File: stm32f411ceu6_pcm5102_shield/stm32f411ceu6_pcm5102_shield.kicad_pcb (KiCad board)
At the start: 2 copper layers, 78 parts, among them J100 Conn_01x04_Pin, J101 Conn_01x04_Pin, J200 AudioJack3_Ground_SwitchTR, J300 AudioJack3_Ground_SwitchTR, Q300 BC337, Q301 BC337, SW100 RotaryEncoder_Switch_MP, SW200 SW_DPDT_XLX, SW201 SW_DPDT_XLX, SW202 SW_DPDT_XLX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

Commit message: Put all items on a board
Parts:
- removed R203: 100kR, Resistor_SMD:R_0805_2012Metric
- removed R204: 10R, Resistor_SMD:R_0805_2012Metric
- J200, J300: footprint Connector_Audio:Jack_3.5mm_PJ311_Horizontal -> stm32f401_pcm5102_shiled_lib:AudioJack_3.5mm_PJ311
- SW101, SW102, SW103, SW104: footprint Button_Switch_THT:SW_PUSH_6mm -> stm32f401_pcm5102_shiled_lib:SW_PUSH_6mm_H5mm
- moved J200 59.2 mm to (193.5, 111.9)
- moved J300 44.1 mm to (192.8, 91.4)
- moved U200 39.3 mm to (144.1, 94.4)
- moved R304 35.6 mm to (168.9, 82.9)
- moved R309 32.7 mm to (173.3, 85.8)
- moved R308 32.7 mm to (173.3, 82.9)
- moved L200 31.1 mm to (146.9, 99.4)
- moved C205 30.3 mm to (136.5, 92.0)
- moved C207 30.3 mm to (136.5, 95.1)
- moved C209 30.3 mm to (136.5, 98.3)
- moved C211 30.3 mm to (136.5, 101.4)
- moved C213 28.8 mm to (131.4, 91.9)
- moved C214 28.8 mm to (131.4, 94.9)
- moved C215 28.8 mm to (131.4, 97.9)
- moved C216 28.8 mm to (131.4, 100.9)
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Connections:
- SW101 pad 1: USR_MIC_MUTE_BTN -> +3.3V
- SW101 pad 2: +3.3V -> USR_MIC_MUTE_BTN
- SW102 pad 1: USR_SCAN_NEXT_BTN -> +3.3V
- SW102 pad 2: +3.3V -> USR_SCAN_NEXT_BTN
- SW103 pad 1: USR_SCAN_PREV_BTN -> +3.3V
- SW103 pad 2: +3.3V -> USR_SCAN_PREV_BTN
- SW104 pad 1: USR_PLAY_PAUSE_BTN -> +3.3V
- SW104 pad 2: +3.3V -> USR_PLAY_PAUSE_BTN

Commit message: PCB rules setup
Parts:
- added J201: Conn_01x03_Pin, Connector_PinHeader_2.54mm:PinHeader_1x03_P2.54mm_Vertical, F.Cu at (129.4, 120.5)
- added J301: Conn_01x03_Pin, Connector_PinHeader_2.54mm:PinHeader_1x03_P2.54mm_Vertical, F.Cu at (141.3, 127.8)
- C100, C101, C102, C204, C206, C208, C210: footprint Capacitor_SMD:C_0805_2012Metric -> Capacitor_SMD:C_0402_1005Metric
- moved J200 91.7 mm to (102.5, 123.0)
- moved D1 59.1 mm to (113.1, 102.5)
- moved J300 53.4 mm to (144.5, 114.0)
- moved L200 53.3 mm to (109.5, 137.3)
- moved U201 44.6 mm to (111.4, 133.3)
- moved C100 43.6 mm to (147.8, 93.0)
- moved C101 42.5 mm to (147.8, 95.0)
- moved C102 41.5 mm to (147.8, 97.0)
- moved U200 39.4 mm to (131.8, 131.8)
- moved C302 30.3 mm to (152.9, 128.8)
- moved R202 30.3 mm to (94.8, 137.3)
- moved SW100 30.3 mm to (124.0, 81.7)
- moved C201 30.3 mm to (110.2, 122.6)
- moved C202 30.3 mm to (110.2, 125.7)
- moved C205 30.3 mm to (124.2, 119.7)
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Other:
- copper layers 2 -> 4
- rule pad_to_mask_clearance: 0 -> 0.038

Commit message: Initial layout
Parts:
- removed C204, C206, C208: 100nF, Capacitor_SMD:C_0402_1005Metric
- removed C205, C207, C209: 10uF, Capacitor_Tantalum_SMD:CP_EIA-3216-18_Kemet-A
- added C1: 100nF, Capacitor_SMD:C_0402_1005Metric, F.Cu at (104.0, 103.5)
- added C2: 100nF, Capacitor_SMD:C_0402_1005Metric, F.Cu at (114.2, 103.8)
- added C3: 100nF, Capacitor_SMD:C_0402_1005Metric, F.Cu at (104.0, 110.1)
- added C4: 10uF, Capacitor_Tantalum_SMD:CP_EIA-3216-18_Kemet-A, F.Cu at (100.8, 103.5)
- added C5: 10uF, Capacitor_Tantalum_SMD:CP_EIA-3216-18_Kemet-A, F.Cu at (117.5, 103.8)
- added C6: 10uF, Capacitor_Tantalum_SMD:CP_EIA-3216-18_Kemet-A, F.Cu at (100.8, 110.1)
- moved R311 68.8 mm to (94.3, 102.6), turned to -90 degrees
- moved R308 67.6 mm to (94.5, 122.3)
- moved R310 67.1 mm to (94.1, 110.9), turned to 90 degrees
- moved R309 67.0 mm to (94.3, 119.8)
- moved J300 63.5 mm to (81.3, 120.9), turned to 90 degrees
- moved C101 58.9 mm to (109.9, 49.9)
- moved R306 58.6 mm to (98.1, 120.7), turned to 90 degrees
- moved C303 58.1 mm to (96.7, 116.9)
- moved Q301 56.3 mm to (102.4, 119.4), turned to 90 degrees
- moved C301 55.9 mm to (97.0, 125.0), turned to 180 degrees
- moved Q300 55.5 mm to (102.3, 127.7), turned to 90 degrees
- moved R302 55.3 mm to (98.2, 128.2), turned to 90 degrees
- moved C102 54.8 mm to (120.4, 49.5)
- moved R307 54.1 mm to (102.7, 114.1)
- moved J301 54.1 mm to (87.2, 128.3), turned to -90 degrees
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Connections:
- SW101 pad 1: +3.3V -> USR_MIC_MUTE_BTN
- SW101 pad 2: USR_MIC_MUTE_BTN -> +3.3V
- SW102 pad 1: +3.3V -> USR_SCAN_NEXT_BTN
- SW102 pad 2: USR_SCAN_NEXT_BTN -> +3.3V
- SW103 pad 1: +3.3V -> USR_SCAN_PREV_BTN
- SW103 pad 2: USR_SCAN_PREV_BTN -> +3.3V
- SW104 pad 1: +3.3V -> USR_PLAY_PAUSE_BTN
- SW104 pad 2: USR_PLAY_PAUSE_BTN -> +3.3V
- U101 pad 1: +3.3V -> +3.3VA
- U200 pad 20: +3.3V -> +3.3VA
- U200 pad 8: +3.3VA -> +3.3V

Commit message: Initial layout
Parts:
- removed Brd100: SSD1306, stm32f401_pcm5102_shiled_lib:128x64OLED
- removed SW201, SW202, SW203, SW204: SW_DPDT_XLX, stm32f401_pcm5102_shiled_lib:SW_DPDT_XLX
- added J102: Conn_01x04_Pin, Connector_PinHeader_2.54mm:PinHeader_1x04_P2.54mm_Vertical, F.Cu at (104.9, 98.8)
- moved D1 86.2 mm to (82.2, 58.0)
- moved R110 80.4 mm to (85.7, 58.0), turned to 0 degrees
- moved U101 66.7 mm to (83.0, 68.1), turned to 180 degrees
- moved J101 44.7 mm to (87.1, 98.8), turned to 90 degrees
- moved C203 39.1 mm to (125.5, 126.5), turned to -90 degrees
- moved C202 29.8 mm to (122.5, 125.7), turned to 180 degrees
- moved U201 23.9 mm to (123.2, 121.5), turned to 90 degrees
- moved R105 20.0 mm to (92.5, 53.2)
- moved R107 19.6 mm to (117.7, 75.8), turned to 0 degrees
- moved R108 19.6 mm to (117.9, 52.5), turned to 0 degrees
- moved R200 19.1 mm to (122.5, 118.0), turned to 180 degrees
- moved R109 18.9 mm to (109.9, 75.8), turned to 0 degrees
- moved R106 18.7 mm to (110.7, 52.5), turned to 0 degrees
- moved SW103 18.6 mm to (116.7, 62.2)
- moved SW102 18.5 mm to (116.7, 72.2)
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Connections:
- U100 pad 26: I2C1_SDA -> /MCU/I2C1_SDA
- U100 pad 27: I2C1_SCL -> /MCU/I2C1_SCL
- U200 pad 10: /PCM5102/DEMP_CFG -> GND
- U200 pad 11: /PCM5102/FLT_CFG -> GND
- U200 pad 16: /PCM5102/FMT_CFG -> GND
- U200 pad 17: /PCM5102/XSMT_CFG -> +3.3V

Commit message: Board outline
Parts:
- added H1: MountingHole, MountingHole:MountingHole_3.2mm_M3, F.Cu at (80.2, 55.0)
- added H2: MountingHole, MountingHole:MountingHole_3.2mm_M3, F.Cu at (130.2, 55.0)
- added H3: MountingHole, MountingHole:MountingHole_3.2mm_M3, F.Cu at (130.2, 132.5)
- added H4: MountingHole, MountingHole:MountingHole_3.2mm_M3, F.Cu at (80.2, 132.5)
- moved R110 5.41 mm to (86.8, 52.7), turned to 90 degrees
- moved D1 4.86 mm to (86.8, 56.2), turned to -90 degrees
- moved SW200 1.58 mm to (127.5, 108.2)
- moved J301 1.00 mm to (82.5, 115.2)
- moved C200 0.99 mm to (121.0, 97.7)
- moved C201 0.99 mm to (121.0, 99.9)
- moved L200 0.99 mm to (118.5, 98.7)
- moved J300 0.96 mm to (79.8, 123.0)
- moved J200 0.77 mm to (79.8, 107.9)
- moved C100 0.77 mm to (98.2, 75.4)
- moved C202 0.77 mm to (122.0, 125.1)
- moved C203 0.77 mm to (125.0, 125.9)
- moved J101 0.77 mm to (86.6, 98.2)
- moved J102 0.77 mm to (104.4, 98.2)
- moved R100 0.77 mm to (95.9, 74.4)
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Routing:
- net Net-(J100-Pin_4): track 0.00 -> 7.95 mm
- net Net-(J100-Pin_3): track 0.00 -> 7.95 mm
- net Net-(J100-Pin_2): track 0.00 -> 7.95 mm
- net Net-(J100-Pin_1): track 0.00 -> 7.95 mm
- net +5V: track 0.00 -> 5.59 mm
- net /MCU/I2C1_SCL: track 0.00 -> 4.25 mm
- net /MCU/I2C1_SDA: track 0.00 -> 4.25 mm
- net /MCU/USART1_RX: track 0.00 -> 4.24 mm
- net /MCU/USART1_TX: track 0.00 -> 4.24 mm
- net GND: track 0.00 -> 3.70 mm
- net +5VA: track 0.00 -> 2.02 mm
- added copper zone on In1.Cu, net GND
- added copper zone on In2.Cu, net GND
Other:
- board outline added: 60 x 87.5 mm

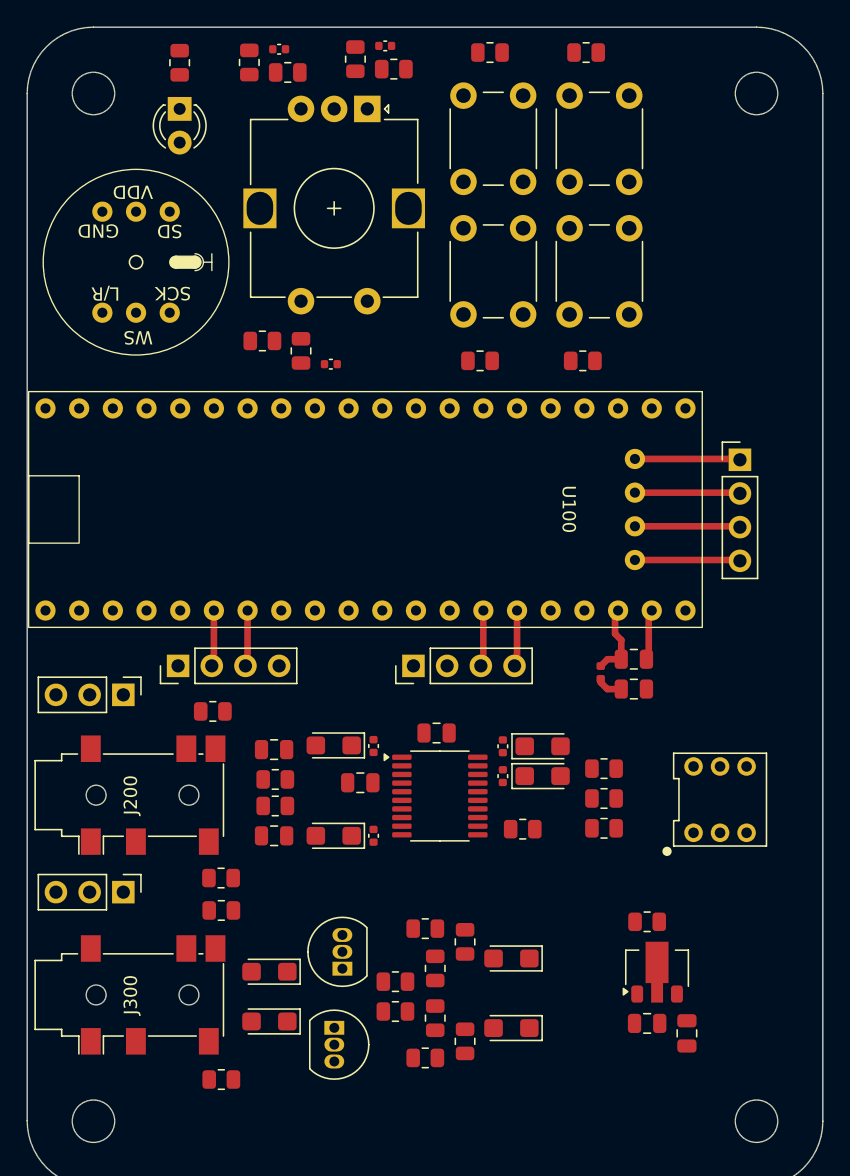
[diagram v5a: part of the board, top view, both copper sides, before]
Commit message: First PCB routing
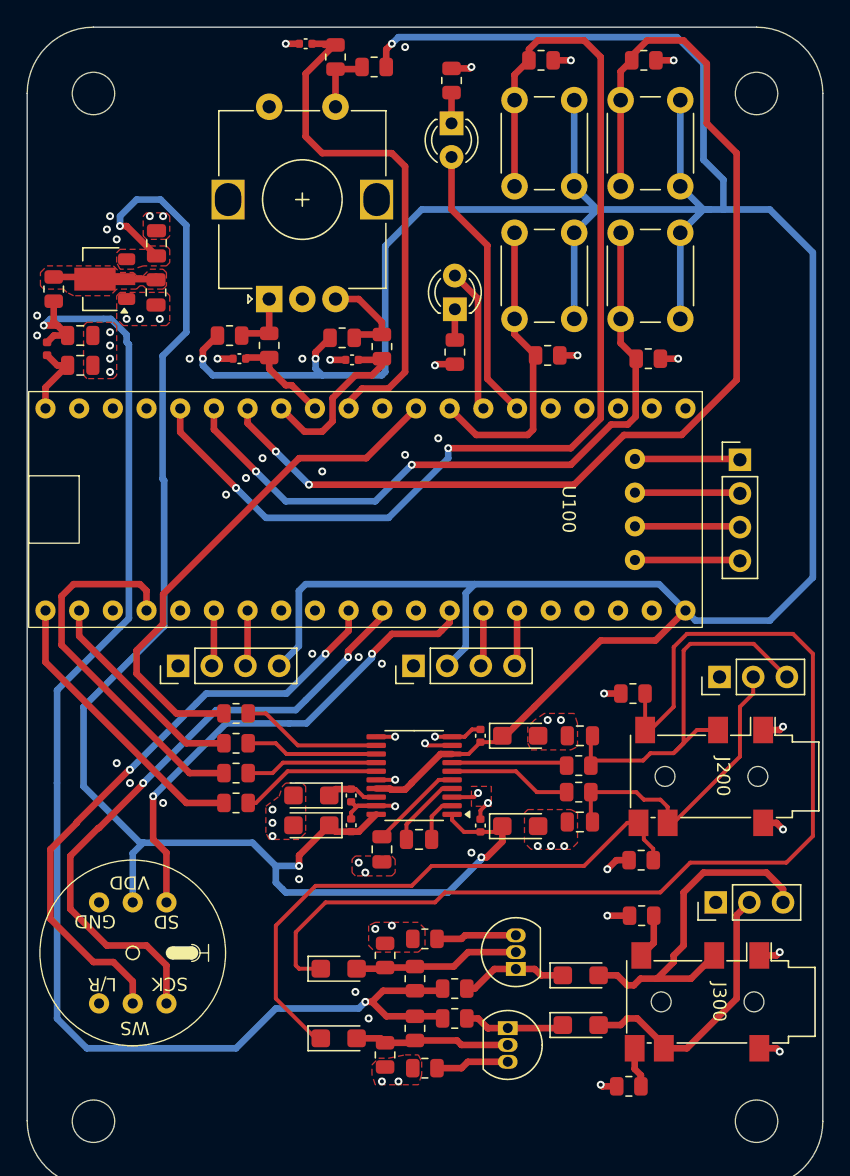
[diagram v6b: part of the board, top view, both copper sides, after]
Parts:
- removed SW200: SW_DPDT_XLX, stm32f401_pcm5102_shiled_lib:SW_DPDT_XLX
- added D101: LED, LED_THT:LED_D3.0mm, F.Cu at (107.2, 57.2)
- added R111: 1kR, Resistor_SMD:R_0805_2012Metric, F.Cu at (107.2, 54.0)
- moved C203 71.8 mm to (85.0, 66.3), turned to 90 degrees
- moved U201 66.8 mm to (80.8, 69.0), turned to 180 degrees
- moved C202 66.4 mm to (85.0, 70.0), turned to -90 degrees
- moved R200 65.4 mm to (77.2, 69.8), turned to -90 degrees
- moved U101 52.1 mm to (83.2, 119.8)
- moved J200 51.3 mm to (131.0, 106.5), turned to -90 degrees
- moved J300 51.0 mm to (130.8, 123.5), turned to -90 degrees
- moved C201 49.5 mm to (79.2, 73.2)
- moved L200 48.4 mm to (76.8, 74.2), turned to 90 degrees
- moved C200 47.3 mm to (79.2, 75.5)
- moved J201 45.0 mm to (127.5, 99.0), turned to 90 degrees
- moved J301 44.7 mm to (127.2, 116.0), turned to 90 degrees
- moved R311 34.2 mm to (121.5, 112.8), turned to 0 degrees
- moved R310 34.0 mm to (120.9, 100.2), turned to 0 degrees
- moved R308 34.0 mm to (121.6, 117.0), turned to 180 degrees
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- renumbered D1 to D100
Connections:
- R10 pad 1: /PCM5102/SCK_CFG -> I2S2_MCK
- R103 pad 2: Net-(R102-Pad2) -> Net-(R103-Pad2)
- R105 pad 1: Net-(R102-Pad2) -> Net-(R103-Pad2)
- SW100 pad A: Net-(R102-Pad2) -> Net-(R103-Pad2)
- U100 pad 19: unconnected-(U100-GND-Pad19) -> GND
- U100 pad 20: unconnected-(U100-5V-Pad20) -> +5V
- U100 pad 23: +5V -> unconnected-(U100-5V-Pad23)
- U100 pad 6: unconnected-(U100-PA0-Pad6) -> LED_SPK_MUTE
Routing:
- net +3.3V: track 0.00 -> 247.2 mm, vias 0 -> 3
- net +3.3VA: track 0.00 -> 114.5 mm, vias 0 -> 3
- net +5VA: track 2.02 -> 105.4 mm, vias 0 -> 2
- net USR_SCAN_NEXT_BTN: track 0.00 -> 85.0 mm, vias 0 -> 2
- net USR_PLAY_PAUSE_BTN: track 0.00 -> 84.0 mm, vias 0 -> 2
- net NO_AMP_R_CONNECTED: track 0.00 -> 81.9 mm
- net USR_SCAN_PREV_BTN: track 0.00 -> 52.6 mm, vias 0 -> 2
- net I2S3_CK: track 0.00 -> 47.7 mm, vias 0 -> 2
- net I2S3_WS: track 0.00 -> 46.0 mm, vias 0 -> 2
- net NO_AMP_L_CONNECTED: track 0.00 -> 44.0 mm
- net USR_SPK_MUTE_BTN: track 0.00 -> 40.2 mm
- net GND: track 3.70 -> 43.3 mm, vias 0 -> 71
- net I2S2_MCK: track 0.00 -> 39.5 mm
- net I2S3_SD: track 0.00 -> 37.3 mm, vias 0 -> 2
- net /PCM5102/NO_AMP_OUT_R: track 0.00 -> 29.9 mm
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- added copper zone on F.Cu, net +3.3VA
- added copper zone on F.Cu, net /PCM5102/+5V_FILT
- added copper zone on F.Cu, net GND

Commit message: Update firmware to simplify routing
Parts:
- added D102: LED, LED_THT:LED_D3.0mm, F.Cu at (107.5, 63.7)
- added R112: 1kR, Resistor_SMD:R_0805_2012Metric, F.Cu at (108.0, 61.2)
- R10, R7, R8, R9: footprint Resistor_SMD:R_0805_2012Metric -> Resistor_SMD:R_0603_1608Metric
- moved R10 13.1 mm to (103.8, 98.8), turned to -90 degrees
- moved R7 12.3 mm to (98.5, 98.8), turned to -90 degrees
- moved R9 12.2 mm to (102.0, 98.8), turned to -90 degrees
- moved R8 11.9 mm to (100.2, 98.8), turned to -90 degrees
- moved R110 5.77 mm to (108.0, 68.8), turned to 0 degrees
- moved J102 4.30 mm to (108.7, 98.5)
- moved D101 1.05 mm to (107.5, 56.2)
- moved R111 0.79 mm to (108.0, 53.8), turned to 0 degrees
- moved D100 0.20 mm to (107.5, 71.1), turned to -90 degrees
- moved J101 0.09 mm to (86.6, 98.2)
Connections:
- R10 pad 1: I2S2_MCK -> I2S3_MCK
- R7 pad 1: I2S2_WS -> I2S3_WS
- R8 pad 1: I2S2_SD -> I2S3_SD
- R9 pad 1: I2S2_CK -> I2S3_CK
- U100 pad 10: unconnected-(U100-PA4-Pad10) -> LED_SPK_MUTE
- U100 pad 14: USR_SCAN_NEXT_BTN -> USR_PLAY_PAUSE_BTN
- U100 pad 16: USR_PLAY_PAUSE_BTN -> USR_SCAN_NEXT_BTN
- U100 pad 17: unconnected-(U100-PB10-Pad17) -> I2S3_MCK
- U100 pad 6: LED_SPK_MUTE -> unconnected-(U100-PA0-Pad6)
- U100 pad 9: I2S2_MCK -> USR_MIC_STREAMING
- U101 pad 3: I2S3_CK -> I2S2_CK
- U101 pad 4: I2S3_SD -> I2S2_SD
- U101 pad 5: I2S3_WS -> I2S2_WS
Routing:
- net I2S3_CK: track 47.7 -> 3.95 mm, vias 2 -> 0
- net I2S3_WS: track 46.0 -> 4.35 mm, vias 2 -> 0
- net I2S3_MCK: track 0.00 -> 40.7 mm
- net I2S2_MCK: track 39.5 -> 0.00 mm
- net I2S3_SD: track 37.3 -> 13.0 mm, vias 2 -> 0
- net I2S2_CK: track 16.2 -> 33.9 mm
- net USR_MIC_STREAMING: track 0.00 -> 13.7 mm
- net I2S2_WS: track 21.7 -> 33.1 mm
- net USR_PLAY_PAUSE_BTN: track 84.0 -> 73.7 mm, vias 2 -> 0
- net USR_SCAN_NEXT_BTN: track 85.0 -> 91.5 mm, vias 2 -> 0
- net I2S2_SD: track 28.4 -> 22.6 mm
- net LED_MIC_MUTE: track 10.9 -> 6.03 mm
- net Net-(D102-K): track 0.00 -> 3.80 mm
- net USR_MIC_MUTE_BTN: track 22.9 -> 26.2 mm
- net /PCM5102/SCK: track 10.7 -> 8.20 mm
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
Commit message: BOM fixes
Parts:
- R303, R307: footprint Resistor_SMD:R_0805_2012Metric -> Resistor_SMD:R_0603_1608Metric
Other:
- board text added: "3V3"
- board text added: "Amplified"
- board text added: "CLK"
- board text added: "DIO"
- board text added: "GLR"
- board text added: "GND"
- board text added: "MIC MUTE"
- board text added: "MIC STREAM"
- board text added: "NO amplification"
- board text added: "PLAY PAUSE"
- board text added: "RX"
- board text added: "SCAN NEXT"
- board text added: "SCAN PREV"
- board text added: "SCL"
- board text added: "SDA"
- board text added: "SPK MUTE"
- board text added: "TX"
- board text added: "Volume control"
